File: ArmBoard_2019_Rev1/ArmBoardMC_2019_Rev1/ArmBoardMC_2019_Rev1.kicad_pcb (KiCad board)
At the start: 2 copper layers, 58 parts, among them U1 VNH5019A_E, U10 Limit_Switch7, U11 Limit_Switch2, U12 Limit_Switch4, U13 Limit_Switch6, U14 Limit_Switch8, U15 MAX_3232, U16 OKI, U17 Encoder_1, U18 Encoder_3, U19 Encoder_2, U2 VNH5019A_E, U20 Encoder_4, U3 TM4C129E_Launchpad, U5 VNH5019A_E, U6 VNH5019A_E, U7 Limit_Switch1, U8 Limit_Switch3, U9 Limit_Switch5

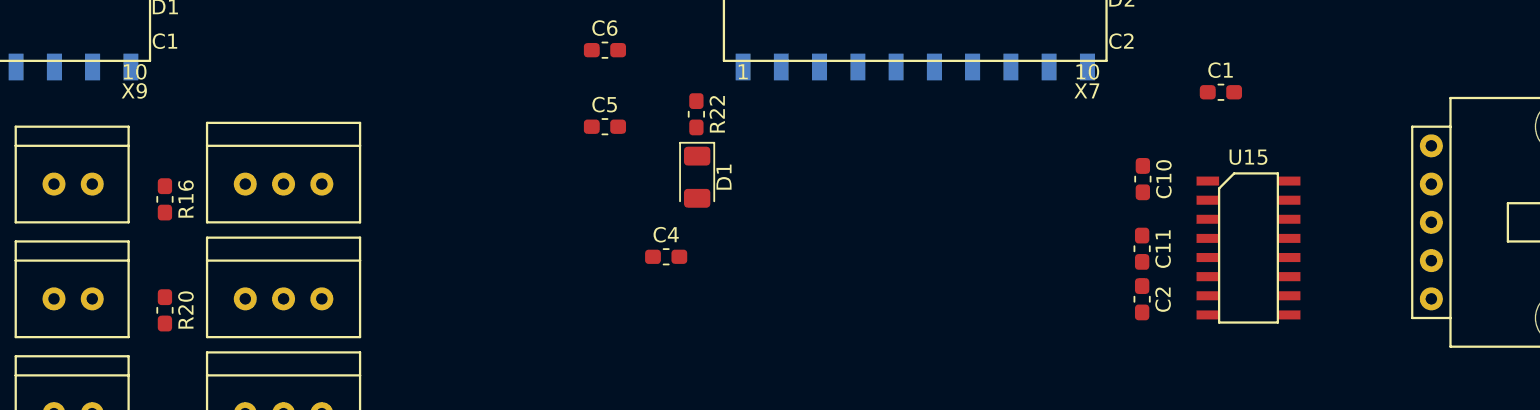
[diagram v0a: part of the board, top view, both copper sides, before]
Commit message: Started wiring armboard
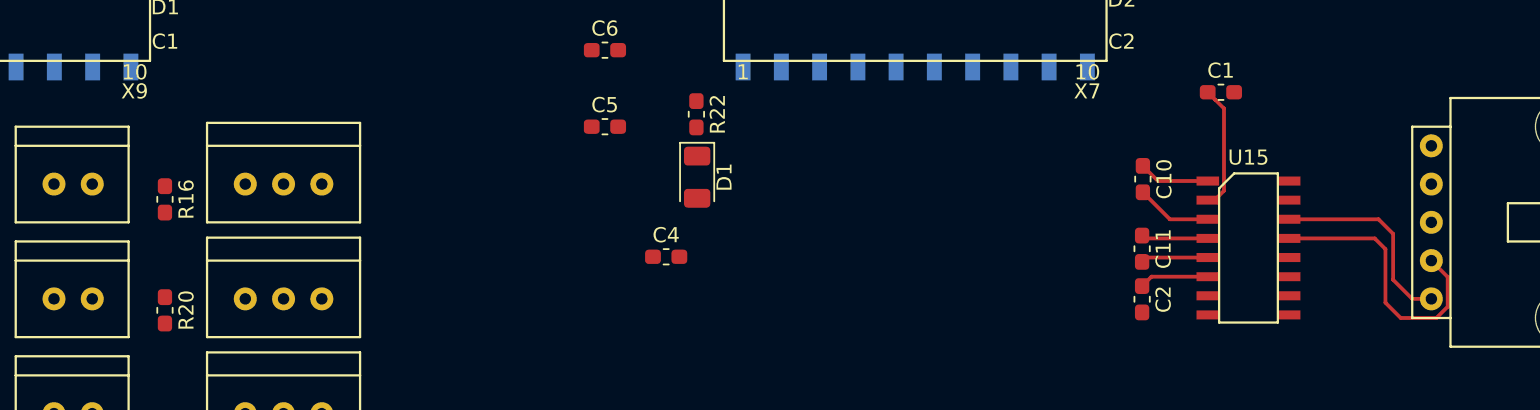
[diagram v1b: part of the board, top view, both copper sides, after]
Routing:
- net RX_1_SL: track 0.00 -> 18.6 mm
- net TX_1_SL: track 0.00 -> 13.4 mm
- net Net-(C1-Pad1): track 0.00 -> 8.32 mm
- net Net-(C10-Pad2): track 0.00 -> 5.05 mm
- net Net-(C10-Pad1): track 0.00 -> 4.73 mm
- net Net-(C2-Pad1): track 0.00 -> 4.62 mm
- net Net-(C11-Pad2): track 0.00 -> 4.48 mm
- net Net-(C11-Pad1): track 0.00 -> 4.44 mm
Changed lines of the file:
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@@
     (thickness 1.6)
     (drawings 0)
-    (tracks 472)
+    (tracks 501)
     (zones 0)
     (modules 58)
@@
     (pad_to_mask_clearance 0.2)
     (aux_axis_origin 0 0)
-    (visible_elements 7FFFF7FF)
+    (visible_elements 7FFFFFFF)
     (pcbplotparams
       (layerselection 0x010fc_ffffffff)
@@
     (add_net VCC_12V)
   )
+  (module MRDT_Connectors:MOLEX_SL_02_Vertical (layer F.Cu)
+    (at 60.198 112.014)
+    (fp_text reference U13 (at -1.905 3.429) (layer F.SilkS) hide
+      (effects (font (size 1 1) (thickness 0.15)))
+    )
+    (fp_text value Limit_Switch6 (at 1.016 3.429) (layer F.Fab)
+      (effects (font (size 1 1) (thickness 0.15)))
+    )
+    (fp_line (start -3.81 -2.54) (end -3.81 2.54) (layer F.SilkS) (width 0.15))
+    (fp_line (start 3.683 -2.54) (end 3.683 2.54) (layer F.SilkS) (width 0.15))
+    (fp_line (start -3.81 -2.54) (end 3.683 -2.54) (layer F.SilkS) (width 0.15))
+    (fp_line (start 3.683 2.54) (end -3.81 2.54) (layer F.SilkS) (width 0.15))
+    (fp_line (start -3.81 -2.54) (end -3.81 -3.81) (layer F.SilkS) (width 0.15))
+    (fp_line (start 3.683 -3.81) (end 3.683 -2.54) (layer F.SilkS) (width 0.15))
+    (fp_line (start -3.81 -3.81) (end 3.683 -3.81) (layer F.SilkS) (width 0.15))
+    (pad 2 thru_hole circle (at 1.27 0) (size 1.524 1.524) (drill 0.762) (layers *.Cu *.Mask)
+      (net 30 LS_6))
+    (pad 1 thru_hole circle (at -1.27 0) (size 1.524 1.524) (drill 0.762) (layers *.Cu *.Mask)
+      (net 32 Logic_3.3V))
+  )
+  (module MRDT_Connectors:MOLEX_SL_02_Vertical (layer F.Cu)
+    (at 50.038 119.634)
+    (fp_text reference U8 (at -1.905 3.429) (layer F.SilkS) hide
+      (effects (font (size 1 1) (thickness 0.15)))
+    )
+    (fp_text value Limit_Switch3 (at 1.016 3.429) (layer F.Fab)
+      (effects (font (size 1 1) (thickness 0.15)))
+    )
+    (fp_line (start -3.81 -3.81) (end 3.683 -3.81) (layer F.SilkS) (width 0.15))
+    (fp_line (start 3.683 -3.81) (end 3.683 -2.54) (layer F.SilkS) (width 0.15))
+    (fp_line (start -3.81 -2.54) (end -3.81 -3.81) (layer F.SilkS) (width 0.15))
+    (fp_line (start 3.683 2.54) (end -3.81 2.54) (layer F.SilkS) (width 0.15))
+    (fp_line (start -3.81 -2.54) (end 3.683 -2.54) (layer F.SilkS) (width 0.15))
+    (fp_line (start 3.683 -2.54) (end 3.683 2.54) (layer F.SilkS) (width 0.15))
+    (fp_line (start -3.81 -2.54) (end -3.81 2.54) (layer F.SilkS) (width 0.15))
+    (pad 1 thru_hole circle (at -1.27 0) (size 1.524 1.524) (drill 0.762) (layers *.Cu *.Mask)
+      (net 32 Logic_3.3V))
+    (pad 2 thru_hole circle (at 1.27 0) (size 1.524 1.524) (drill 0.762) (layers *.Cu *.Mask)
+      (net 27 LS_3))
+  )
   (module Capacitor_SMD:C_0603_1608Metric_Pad1.05x0.95mm_HandSolder (layer F.Cu)
     (at 136.398 98.298)
@@
   )
   (module MRDT_Connectors:MOLEX_SL_02_Vertical (layer F.Cu)
-    (at 50.038 119.634)
-    (fp_text reference U8 (at -1.905 3.429) (layer F.SilkS) hide
-      (effects (font (size 1 1) (thickness 0.15)))
-    )
-    (fp_text value Limit_Switch3 (at 1.016 3.429) (layer F.Fab)
-      (effects (font (size 1 1) (thickness 0.15)))
-    )
-    (fp_line (start -3.81 -3.81) (end 3.683 -3.81) (layer F.SilkS) (width 0.15))
-    (fp_line (start 3.683 -3.81) (end 3.683 -2.54) (layer F.SilkS) (width 0.15))
-    (fp_line (start -3.81 -2.54) (end -3.81 -3.81) (layer F.SilkS) (width 0.15))
-    (fp_line (start 3.683 2.54) (end -3.81 2.54) (layer F.SilkS) (width 0.15))
-    (fp_line (start -3.81 -2.54) (end 3.683 -2.54) (layer F.SilkS) (width 0.15))
-    (fp_line (start 3.683 -2.54) (end 3.683 2.54) (layer F.SilkS) (width 0.15))
-    (fp_line (start -3.81 -2.54) (end -3.81 2.54) (layer F.SilkS) (width 0.15))
-    (pad 1 thru_hole circle (at -1.27 0) (size 1.524 1.524) (drill 0.762) (layers *.Cu *.Mask)
-      (net 32 Logic_3.3V))
-    (pad 2 thru_hole circle (at 1.27 0) (size 1.524 1.524) (drill 0.762) (layers *.Cu *.Mask)
-      (net 27 LS_3))
-  )
-  (module MRDT_Connectors:MOLEX_SL_02_Vertical (layer F.Cu)
     (at 60.198 104.394)
     (fp_text reference U9 (at -1.905 3.429) (layer F.SilkS) hide
@@
   )
   (module MRDT_Connectors:MOLEX_SL_02_Vertical (layer F.Cu)
-    (at 60.198 112.014)
-    (fp_text reference U13 (at -1.905 3.429) (layer F.SilkS) hide
-      (effects (font (size 1 1) (thickness 0.15)))
-    )
-    (fp_text value Limit_Switch6 (at 1.016 3.429) (layer F.Fab)
-      (effects (font (size 1 1) (thickness 0.15)))
-    )
-    (fp_line (start -3.81 -2.54) (end -3.81 2.54) (layer F.SilkS) (width 0.15))
-    (fp_line (start 3.683 -2.54) (end 3.683 2.54) (layer F.SilkS) (width 0.15))
-    (fp_line (start -3.81 -2.54) (end 3.683 -2.54) (layer F.SilkS) (width 0.15))
-    (fp_line (start 3.683 2.54) (end -3.81 2.54) (layer F.SilkS) (width 0.15))
-    (fp_line (start -3.81 -2.54) (end -3.81 -3.81) (layer F.SilkS) (width 0.15))
-    (fp_line (start 3.683 -3.81) (end 3.683 -2.54) (layer F.SilkS) (width 0.15))
-    (fp_line (start -3.81 -3.81) (end 3.683 -3.81) (layer F.SilkS) (width 0.15))
-    (pad 2 thru_hole circle (at 1.27 0) (size 1.524 1.524) (drill 0.762) (layers *.Cu *.Mask)
-      (net 30 LS_6))
-    (pad 1 thru_hole circle (at -1.27 0) (size 1.524 1.524) (drill 0.762) (layers *.Cu *.Mask)
-      (net 32 Logic_3.3V))
-  )
-  (module MRDT_Connectors:MOLEX_SL_02_Vertical (layer F.Cu)
     (at 60.198 127.254)
     (fp_text reference U14 (at -1.905 3.429) (layer F.SilkS) hide
@@
     (pad "" np_thru_hole circle (at 6.35 -8.636 270) (size 3.45 3.45) (drill 3.45) (layers *.Cu *.Mask))
   )
+  (segment (start 61.609 104.535) (end 61.468 104.394) (width 0.25) (layer F.Cu) (net 28))
+  (segment (start 132.2184 104.1908) (end 131.2164 103.1888) (width 0.25) (layer F.Cu) (net 84))
+  (segment (start 135.5268 104.1908) (end 132.2184 104.1908) (width 0.25) (layer F.Cu) (net 84))
+  (segment (start 136.022072 98.797072) (end 135.523 98.298) (width 0.25) (layer F.Cu) (net 85))
+  (segment (start 136.601801 99.376801) (end 136.022072 98.797072) (width 0.25) (layer F.Cu) (net 85))
+  (segment (start 136.601801 104.835799) (end 136.601801 99.376801) (width 0.25) (layer F.Cu) (net 85))
+  (segment (start 135.9768 105.4608) (end 136.601801 104.835799) (width 0.25) (layer F.Cu) (net 85))
+  (segment (start 135.5268 105.4608) (end 135.9768 105.4608) (width 0.25) (layer F.Cu) (net 85))
+  (segment (start 133.0084 106.7308) (end 131.2164 104.9388) (width 0.25) (layer F.Cu) (net 86))
+  (segment (start 135.5268 106.7308) (end 133.0084 106.7308) (width 0.25) (layer F.Cu) (net 86))
+  (segment (start 131.3548 108.0008) (end 131.1656 107.8116) (width 0.25) (layer F.Cu) (net 87))
+  (segment (start 135.5268 108.0008) (end 131.3548 108.0008) (width 0.25) (layer F.Cu) (net 87))
+  (segment (start 131.4564 109.2708) (end 131.1656 109.5616) (width 0.25) (layer F.Cu) (net 88))
+  (segment (start 135.5268 109.2708) (end 131.4564 109.2708) (width 0.25) (layer F.Cu) (net 88))
+  (segment (start 131.7892 110.5408) (end 131.1656 111.1644) (width 0.25) (layer F.Cu) (net 89))
+  (segment (start 135.5268 110.5408) (end 131.7892 110.5408) (width 0.25) (layer F.Cu) (net 89))
+  (segment (start 151.455001 112.535761) (end 150.706762 113.284) (width 0.25) (layer F.Cu) (net 94))
+  (segment (start 150.368 109.474) (end 151.455001 110.561001) (width 0.25) (layer F.Cu) (net 94))
+  (segment (start 151.455001 110.561001) (end 151.455001 112.535761) (width 0.25) (layer F.Cu) (net 94))
+  (segment (start 150.706762 113.284) (end 148.336 113.284) (width 0.25) (layer F.Cu) (net 94))
+  (segment (start 148.336 113.284) (end 147.32 112.268) (width 0.25) (layer F.Cu) (net 94))
+  (segment (start 147.32 112.268) (end 147.32 108.712) (width 0.25) (layer F.Cu) (net 94))
+  (segment (start 146.6088 108.0008) (end 140.9268 108.0008) (width 0.25) (layer F.Cu) (net 94))
+  (segment (start 147.32 108.712) (end 146.6088 108.0008) (width 0.25) (layer F.Cu) (net 94))
+  (segment (start 150.368 112.014) (end 149.098 112.014) (width 0.25) (layer F.Cu) (net 95))
+  (segment (start 149.098 112.014) (end 147.828 110.744) (width 0.25) (layer F.Cu) (net 95))
+  (segment (start 147.828 110.744) (end 147.828 107.696) (width 0.25) (layer F.Cu) (net 95))
+  (segment (start 146.8628 106.7308) (end 140.9268 106.7308) (width 0.25) (layer F.Cu) (net 95))
+  (segment (start 147.828 107.696) (end 146.8628 106.7308) (width 0.25) (layer F.Cu) (net 95))
   (via (at 148.336 71.628) (size 0.8) (drill 0.4) (layers F.Cu B.Cu) (net 98))
   (via (at 125.984 71.628) (size 0.8) (drill 0.4) (layers F.Cu B.Cu) (net 98))

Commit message: Generated new netlist
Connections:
- net Net-(Conn5-Pad1) renamed RX_2_SL
- net Net-(Conn5-Pad2) renamed TX_2_SL
- R9 pad 2: IN_A4 -> IN_B4
- U3 pad PC4: RX_1_Tiva -> Net-(U3-PadPC4)
- U3 pad PC5: TX_1_Tiva -> Net-(U3-PadPC5)
- U3 pad PH0: Net-(U3-PadPH0) -> IN_A3
- U3 pad PH1: Net-(U3-PadPH1) -> IN_A4
- U3 pad PK2: Net-(U3-PadPK2) -> Encoder1_PWM
- U3 pad PK3: Net-(U3-PadPK3) -> Encoder2_PWM
- U3 pad PK6: Net-(U3-PadPK6) -> IN_B3
- U3 pad PK7: Net-(U3-PadPK7) -> IN_B4
- U3 pad PL2: IN_A3 -> Net-(U3-PadPL2)
- U3 pad PL3: IN_A4 -> Net-(U3-PadPL3)
- U3 pad PL4: Encoder1_PWM -> Net-(U3-PadPL4)
- U3 pad PL5: Encoder2_PWM -> Net-(U3-PadPL5)
- U3 pad PN2: IN_B3 -> Net-(U3-PadPN2)
- U3 pad PN3: IN_B4 -> Net-(U3-PadPN3)
- U3 pad PP0: Net-(U3-PadPP0) -> RX_1_Tiva
- U3 pad PP1: Net-(U3-PadPP1) -> TX_1_Tiva

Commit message: Worked on wiring
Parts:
- moved U16 15.7 mm to (84.3, 136.4), turned to 0 degrees
- moved U17 11.6 mm to (79.8, 97.3)
- moved U19 11.6 mm to (79.8, 104.9)
- moved U20 11.6 mm to (79.8, 120.1)
- moved U18 11.6 mm to (79.8, 112.5)
- moved C11 2.09 mm to (129.1, 108.2)
- moved C2 2.09 mm to (129.1, 111.5)
- moved C10 2.03 mm to (129.2, 104.1)
- moved R10 1.61 mm to (148.0, 84.7)
- moved R7 1.61 mm to (151.3, 84.7)
- moved R9 1.61 mm to (154.7, 84.7)
- moved R11 1.44 mm to (128.8, 85.2)
- moved R12 1.44 mm to (132.2, 85.2)
- moved R13 1.44 mm to (125.3, 85.2)
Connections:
- U15 pad 10: Net-(U15-Pad10) -> TX_2_Tiva
- U15 pad 7: Net-(U15-Pad7) -> TX_2_SL
- U15 pad 8: Net-(U15-Pad8) -> RX_2_SL
- U15 pad 9: Net-(U15-Pad9) -> RX_2_Tiva
- U3 pad PA4: Net-(U3-PadPA4) -> RX_2_Tiva
- U3 pad PA5: Net-(U3-PadPA5) -> TX_2_Tiva
- U3 pad PB4: Net-(U3-PadPB4) -> MOTOR3_PWM
- U3 pad PB5: Net-(U3-PadPB5) -> MOTOR4_PWM
- U3 pad PE2: I_Sense_3 -> Net-(U3-PadPE2)
- U3 pad PE3: I_Sense_4 -> Net-(U3-PadPE3)
- U3 pad PF1: MOTOR3_PWM -> Net-(U3-PadPF1)
- U3 pad PG0: MOTOR4_PWM -> Net-(U3-PadPG0)
- U3 pad PK0: Net-(U3-PadPK0) -> I_Sense_3
- U3 pad PK1: Net-(U3-PadPK1) -> I_Sense_4
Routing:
- net RX_1_Tiva: track 0.00 -> 69.1 mm, vias 0 -> 1
- net TX_1_Tiva: track 0.00 -> 63.7 mm, vias 0 -> 1
- net TX_2_Tiva: track 0.00 -> 40.2 mm, vias 0 -> 1
- net RX_2_Tiva: track 0.00 -> 38.8 mm, vias 0 -> 1
- net IN_B4: track 0.00 -> 37.2 mm, vias 0 -> 1
- net RX_2_SL: track 0.00 -> 33.7 mm, vias 0 -> 2
- net IN_A4: track 0.00 -> 33.7 mm, vias 0 -> 1
- net TX_2_SL: track 0.00 -> 30.8 mm, vias 0 -> 2
- net IN_B3: track 0.00 -> 16.4 mm, vias 0 -> 1
- net Logic_3.3V: track 0.00 -> 13.8 mm
- net RX_1_SL: track 18.6 -> 10.1 mm
- net Net-(R12-Pad1): track 0.00 -> 5.81 mm
- net Net-(R13-Pad1): track 0.00 -> 5.74 mm
- net Net-(R11-Pad1): track 0.00 -> 5.64 mm
- net Net-(R9-Pad1): track 0.00 -> 5.25 mm
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
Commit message: Worked on wiring some more
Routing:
- net VCC_12V: track 0.00 -> 99.0 mm
- net Encoder2_PWM: track 0.00 -> 61.8 mm, vias 0 -> 3
- net Encoder3_PWM: track 0.00 -> 54.5 mm, vias 0 -> 3
- net /V+Log: track 0.00 -> 39.3 mm
- net LOGIC_3.3V: track 0.00 -> 22.9 mm
- net Net-(D1-Pad2): track 0.00 -> 11.0 mm, vias 0 -> 2
- net LS_1: track 0.00 -> 10.2 mm
- net Net-(R6-Pad1): track 0.00 -> 7.08 mm
- net Net-(R5-Pad1): track 0.00 -> 6.92 mm
- net Net-(R4-Pad1): track 0.00 -> 6.86 mm
- net Net-(R3-Pad1): track 0.00 -> 6.75 mm
- net Net-(R1-Pad1): track 0.00 -> 6.61 mm
- net Net-(R2-Pad1): track 0.00 -> 6.49 mm
- net Logic_3.3V: track 13.8 -> 20.1 mm
- net LS_7: track 0.00 -> 5.09 mm
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
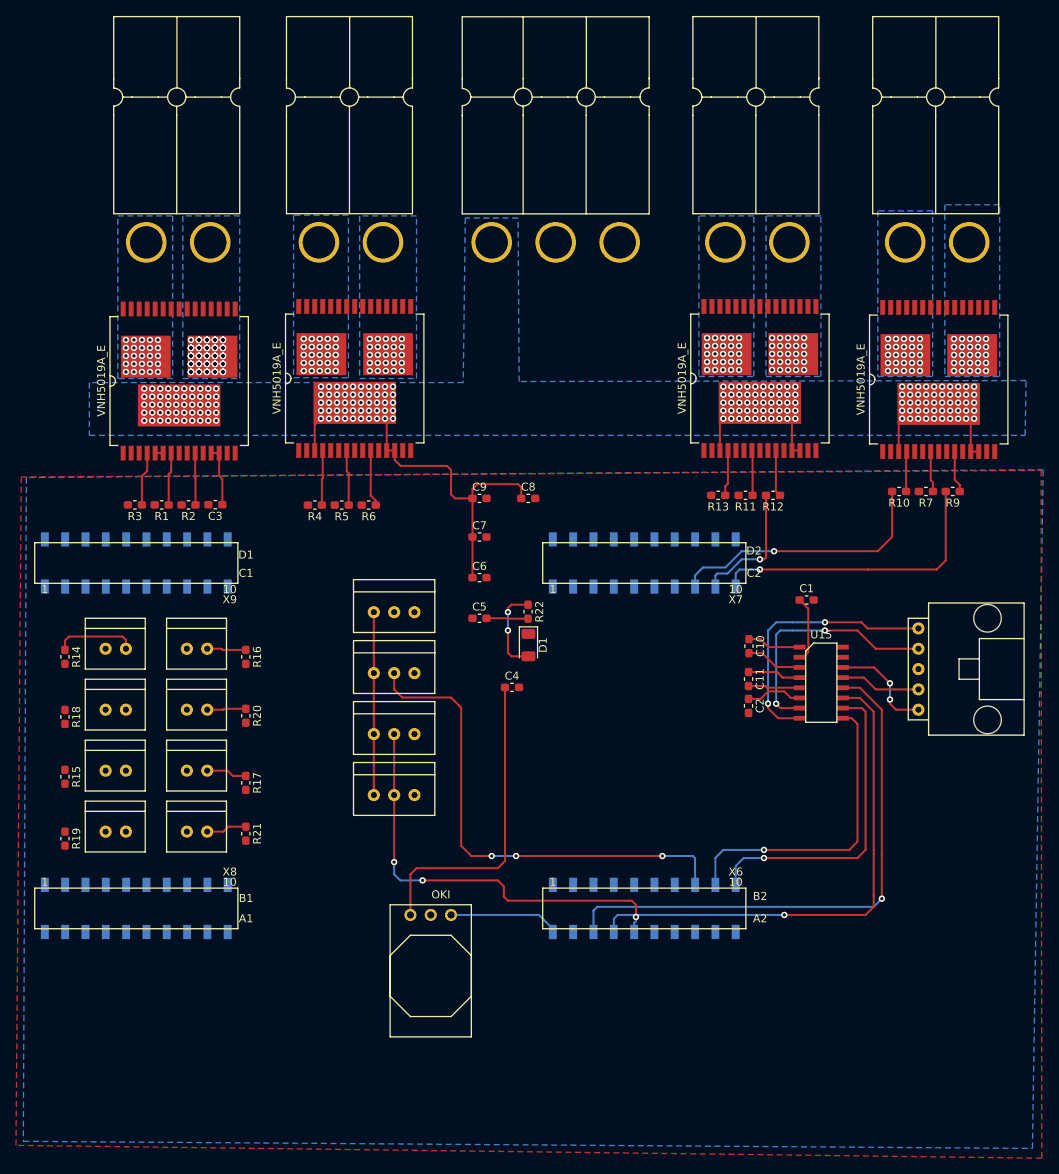
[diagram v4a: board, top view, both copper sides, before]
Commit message: Continued wiring
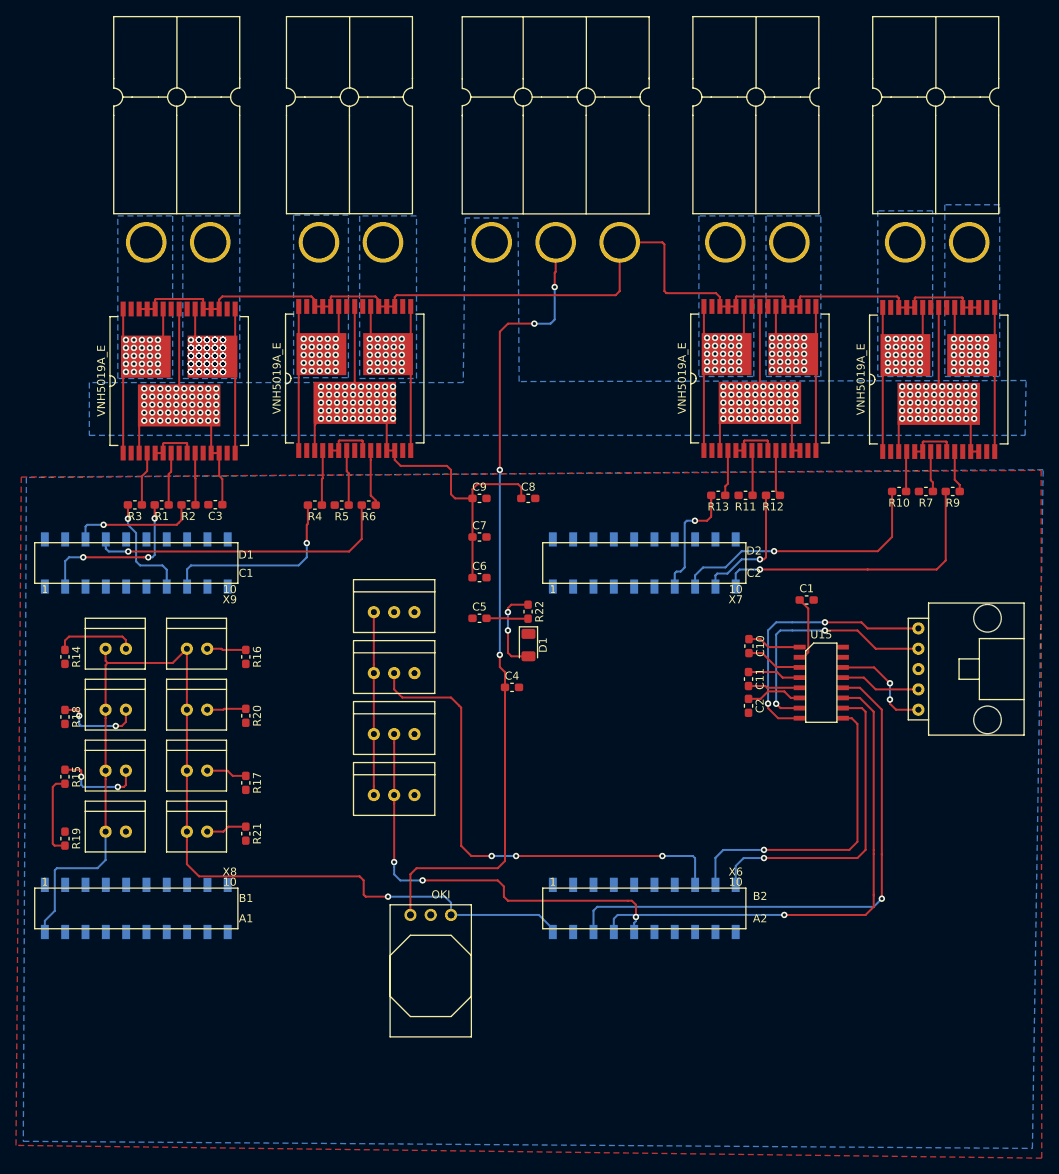
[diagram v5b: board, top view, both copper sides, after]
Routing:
- net GND: track 0.00 -> 144.6 mm
- net Logic_3.3V: track 20.1 -> 161.6 mm, vias 0 -> 1
- net VCC_12V: track 99.0 -> 165.4 mm
- net /V+Log: track 39.3 -> 101.2 mm, vias 0 -> 4
- net IN_B2: track 0.00 -> 38.2 mm, vias 0 -> 1
- net /Out_A1: track 0.00 -> 29.7 mm
- net /Out_B3: track 0.00 -> 29.7 mm
- net /Out_A2: track 0.00 -> 29.1 mm
- net /Out_B2: track 0.00 -> 28.9 mm
- net /Out_B1: track 0.00 -> 28.8 mm
- net /Out_B4: track 0.00 -> 28.8 mm
- net /Out_A3: track 0.00 -> 28.6 mm
- net /Out_A4: track 0.00 -> 28.5 mm
- net IN_A2: track 0.00 -> 24.3 mm, vias 0 -> 1
- net MOTOR1_PWM: track 0.00 -> 20.9 mm, vias 0 -> 3
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
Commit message: Finished wiring
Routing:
- net Logic_3.3V: track 161.6 -> 307.7 mm, vias 1 -> 10
- net I_Sense_1: track 0.00 -> 102.7 mm, vias 0 -> 3
- net I_Sense_2: track 0.00 -> 98.4 mm, vias 0 -> 3
- net MOTOR4_PWM: track 0.00 -> 89.0 mm, vias 0 -> 1
- net I_Sense_4: track 0.00 -> 87.8 mm, vias 0 -> 3
- net Net-(U3-PadRese): track 0.00 -> 84.6 mm
- net Net-(U3-Pad+5V): track 0.00 -> 74.1 mm, vias 0 -> 2
- net I_Sense_3: track 0.00 -> 73.6 mm, vias 0 -> 3
- net Encoder1_PWM: track 0.00 -> 66.9 mm, vias 0 -> 1
- net MOTOR3_PWM: track 0.00 -> 62.7 mm, vias 0 -> 1
- net LS_5: track 5.08 -> 64.4 mm, vias 0 -> 1
- net GND: track 144.6 -> 201.2 mm, vias 0 -> 5
- net LS_6: track 4.87 -> 52.0 mm, vias 0 -> 1
- net LS_1: track 10.2 -> 52.0 mm, vias 0 -> 3
- net LS_2: track 11.1 -> 41.2 mm, vias 2 -> 5
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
